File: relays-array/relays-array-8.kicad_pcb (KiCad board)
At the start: 2 copper layers, 223 x 60 mm, 62 parts, among them J1 NMJ6HCD2, J10 Screw_Terminal_01x02, J11 NMJ6HCD2, J12 NMJ6HCD2, J13 Screw_Terminal_01x02, J14 NMJ6HCD2, J15 Screw_Terminal_01x02, J2 NMJ6HCD2, J3 Screw_Terminal_01x02, J4 NMJ6HCD2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

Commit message: relays-array: add terminal block for buffer use w/ external connector
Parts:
- removed REF**: OSHW-Logo2_7.3x6mm_SilkScreen, Symbol:OSHW-Logo2_7.3x6mm_SilkScreen
- added J16: Screw_Terminal_01x02, TerminalBlock:TerminalBlock_bornier-2_P5.08mm, F.Cu at (50.2, 114.5)
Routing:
- net Net-(J16-Pin_2): track 21.2 -> 29.1 mm

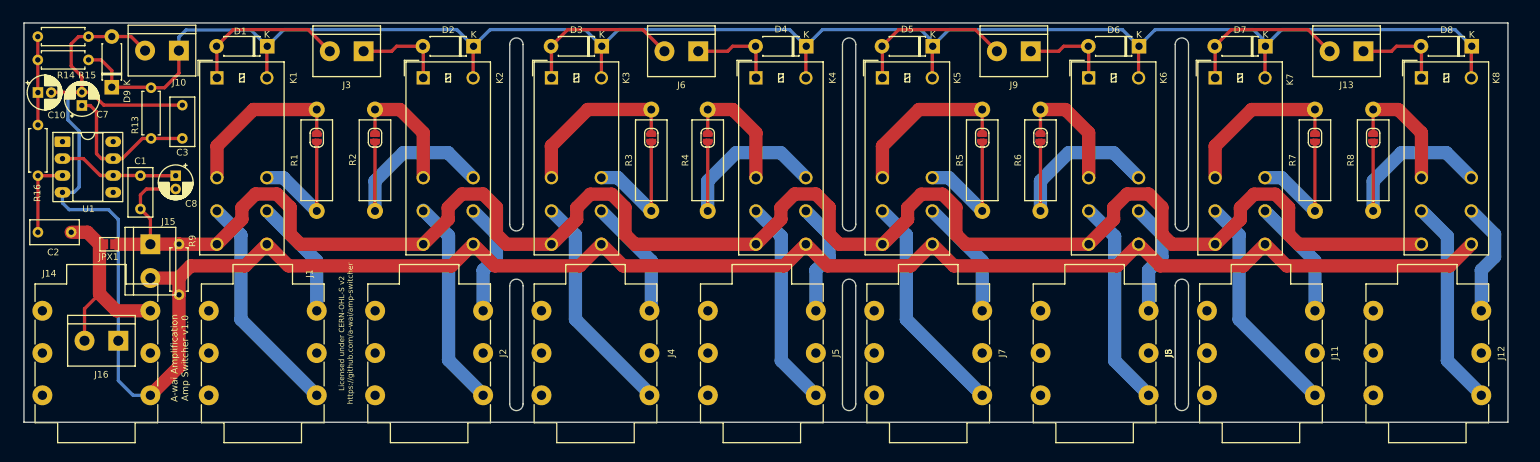
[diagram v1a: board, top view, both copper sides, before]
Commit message: relays-array: add terminal block labels on silkscreen
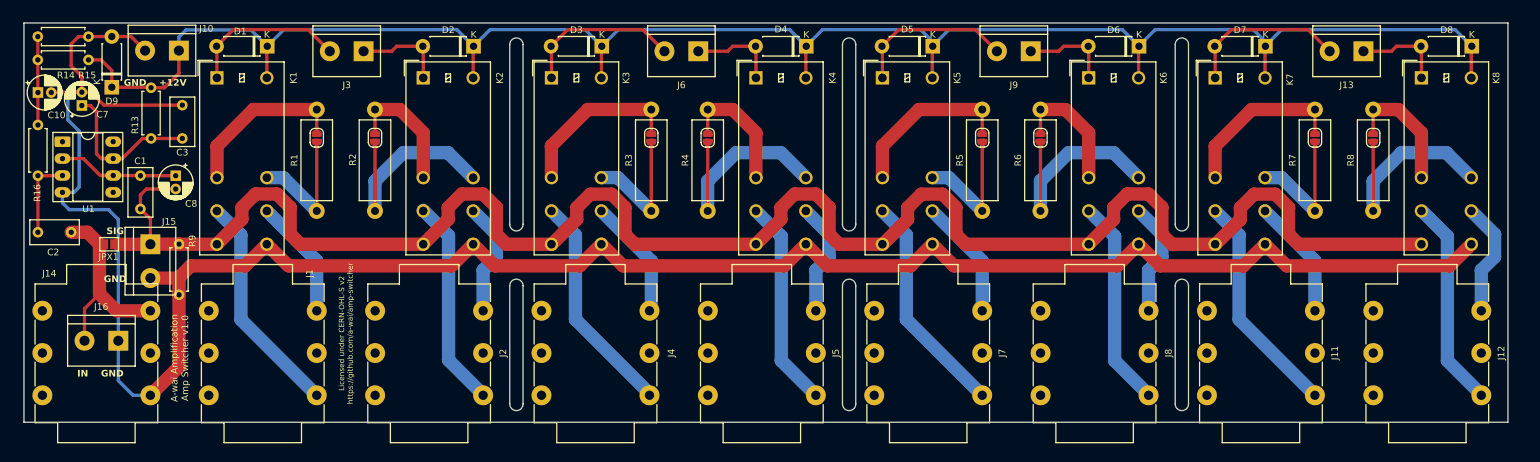
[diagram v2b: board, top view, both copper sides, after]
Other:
- board text added: "GND"
- board text added: "GND +12V"
- board text added: "IN GND"
- board text added: "SIG"
- board text removed: "J5"
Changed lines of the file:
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@@
 		(tags "terminal block bornier2")
 		(property "Reference" "J16"
-			(at 2.54 -5.08 0)
+			(at 2.58 5.1 0)
 			(layer "F.SilkS")
 			(effects
@@
 		(tags "Diode DO-41_SOD81 series Axial Horizontal pin pitch 7.62mm  length 5.2mm diameter 2.7mm")
 		(property "Reference" "D9"
-			(at -1.39 2.3 90)
+			(at -2.09 0 180)
 			(layer "F.SilkS")
 			(effects
@@
 		)
 		(fp_text user "K"
-			(at 0.71 2.3 90)
+			(at 0.81 -2.2 90)
 			(layer "F.SilkS")
 			(effects
@@
 		(tags "terminal block bornier2")
 		(property "Reference" "J15"
-			(at -3.4 -2.7 0)
+			(at -3.4 -2.8 0)
 			(layer "F.SilkS")
 			(effects
@@
 		(tags "terminal block bornier2")
 		(property "Reference" "J10"
-			(at -0.02 -4.8 0)
+			(at -4.12 3.3 0)
 			(layer "F.SilkS")
 			(effects
@@
 		(layer "Edge.Cuts")
 	)
+	(gr_text "GND"
+		(at 48 105.8 0)
+		(layer "F.SilkS")
+		(effects
+			(font
+				(size 1 1)
+				(thickness 0.2)
+				(bold yes)
+			)
+			(justify left bottom)
+		)
+	)
+	(gr_text "GND    +12V"
+		(at 51 76.3 0)
+		(layer "F.SilkS")
+		(effects
+			(font
+				(size 1 1)
+				(thickness 0.2)
+				(bold yes)
+			)
+			(justify left bottom)
+		)
+	)
 	(gr_text "Licensed under CERN-OHL-S v2\nhttps://github.com/a-wai/amp-switcher"
 		(at 85.5 113.4 90)
@@
 		)
 	)
+	(gr_text "IN    GND"
+		(at 44 120 0)
+		(layer "F.SilkS")
+		(effects
+			(font
+				(size 1 1)
+				(thickness 0.2)
+				(bold yes)
+			)
+			(justify left bottom)
+		)
+	)
 	(gr_text "A-wai Amplification\nAmp Switcher v1.0"
 		(at 60.8 117.1 90)
@@
 		)
 	)
-	(gr_text "J5"
-		(at 208 116.35 90)
+	(gr_text "SIG"
+		(at 48.4 98.6 0)
 		(layer "F.SilkS")
 		(effects
 			(font
 				(size 1 1)
-				(thickness 0.15)
+				(thickness 0.2)
+				(bold yes)
 			)
+			(justify left bottom)
 		)
 	)

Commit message: relays-array: fix schematics error and add ground plane
The jack connectors are all (except for the buffer input) wired
backwards, with the tip going to `GND` and the sleeve on `SIGNAL`, while
it should be the other way around.

While at it, improve a bit the PCB tracks and add a ground plane. The
latter is only connected to `GND` in a single point in order to avoid
ground loops and other unpleasant issues.
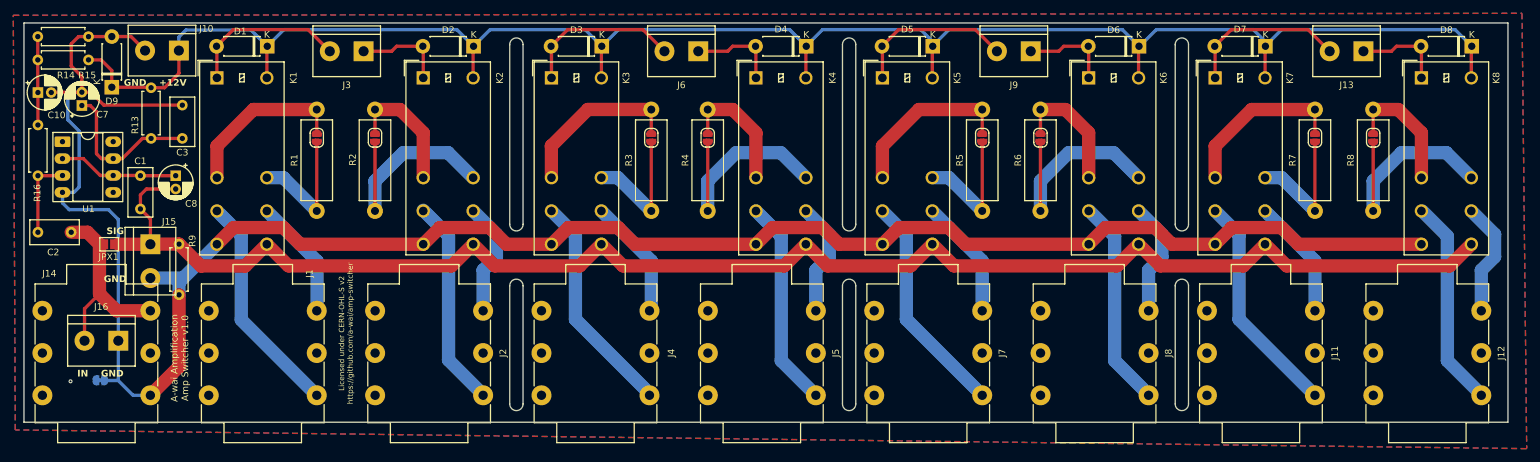
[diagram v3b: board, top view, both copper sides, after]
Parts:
- added JP1: Jumper_2_Bridged, Jumper:SolderJumper-2_P1.3mm_Bridged_RoundedPad1.0x1.5mm, B.Cu at (47.5, 120.4)
- moved JP8 8.75 mm to (238.8, 84.0)
- moved JP9 8.75 mm to (230.0, 84.0)
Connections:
- K1 pad 14: /SIGNAL -> GND
- K1 pad 24: GND -> /SIGNAL
- K2 pad 14: /SIGNAL -> GND
- K2 pad 24: GND -> /SIGNAL
- K3 pad 14: /SIGNAL -> GND
- K3 pad 24: GND -> /SIGNAL
- K4 pad 14: /SIGNAL -> GND
- K4 pad 24: GND -> /SIGNAL
- K5 pad 14: /SIGNAL -> GND
- K5 pad 24: GND -> /SIGNAL
- K6 pad 14: /SIGNAL -> GND
- K6 pad 24: GND -> /SIGNAL
- K7 pad 12: Net-(JP8-A) -> Net-(JP9-A)
- K7 pad 14: /SIGNAL -> GND
- K7 pad 22: Net-(JP8-B) -> Net-(JP9-B)
- K7 pad 24: GND -> /SIGNAL
- K8 pad 12: Net-(JP9-A) -> Net-(JP8-A)
- K8 pad 14: /SIGNAL -> GND
- K8 pad 22: Net-(JP9-B) -> Net-(JP8-B)
- K8 pad 24: GND -> /SIGNAL
- R7 pad 1: Net-(JP8-B) -> Net-(JP9-B)
- R7 pad 2: Net-(JP8-A) -> Net-(JP9-A)
- R8 pad 1: Net-(JP9-B) -> Net-(JP8-B)
- R8 pad 2: Net-(JP9-A) -> Net-(JP8-A)
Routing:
- net /SIGNAL: track 277.1 -> 238.6 mm
- net Net-(JP9-B): track 32.9 -> 19.9 mm
- net Net-(JP8-B): track 19.9 -> 32.9 mm
- net GND: track 340.2 -> 330.7 mm
- net Net-(JP9-A): track 19.0 -> 25.6 mm
- net Net-(JP8-A): track 25.6 -> 19.0 mm
- net Earth: vias 0 -> 1
- added copper zone on B.Cu, net Earth
- added copper zone on F.Cu, net Earth
